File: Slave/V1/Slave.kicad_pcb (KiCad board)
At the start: 2 copper layers, 526 parts, among them J101 649002227222, J102 649002227222, J1301 649002227222, J1701 649002227222, J201 Header_Male_Pin_2.54mm_1X6_,_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, J202 Header_Male_Pin_2.54mm_1X3_,_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, J2101 649002227222, J2501 649002227222, J2901 649002227222, J300 Header_Male_Pin_2.54mm_1X2_,_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, J3301 649002227222, J401 649006227222, J402 649006227222, J501 649002227222, J901 649002227222, Q101 2N7002P,215, Q1201 CPH6347-TL-W, Q1202 BSS806NH6327XTSA1, Q1301 CPH6347-TL-W, Q1302 CPH6347-TL-W, Q1601 CPH6347-TL-W, Q1602 BSS806NH6327XTSA1, Q1701 CPH6347-TL-W, Q1702 CPH6347-TL-W, Q2001 CPH6347-TL-W, Q2002 BSS806NH6327XTSA1, Q2101 CPH6347-TL-W, Q2102 CPH6347-TL-W, Q2401 CPH6347-TL-W, Q2402 BSS806NH6327XTSA1, Q2501 CPH6347-TL-W, Q2502 CPH6347-TL-W, Q2801 CPH6347-TL-W, Q2802 BSS806NH6327XTSA1, Q2901 CPH6347-TL-W, Q2902 CPH6347-TL-W, Q3201 CPH6347-TL-W, Q3202 BSS806NH6327XTSA1, Q3301 CPH6347-TL-W, Q3302 CPH6347-TL-W, Q3601 CPH6347-TL-W, Q3602 BSS806NH6327XTSA1, Q501 CPH6347-TL-W, Q502 CPH6347-TL-W, Q801 CPH6347-TL-W, Q802 BSS806NH6327XTSA1, Q901 CPH6347-TL-W, Q902 CPH6347-TL-W, SW201 PTS645SM43SMTR92, SW202 PTS645SM43SMTR92, U1001 AP3015KTR-G1, U1002 AP2202K-ADJTRG1, U1101 ADC121S021CIMF/NOPB, U1201 ADCMP350YKSZ-REEL7, U1301 LTV-816S, U1302 SI8641AB-B-IS1, U1401 AP3015KTR-G1, U1402 AP2202K-ADJTRG1, U1501 ADC121S021CIMF/NOPB, U1601 ADCMP350YKSZ-REEL7, U1701 LTV-816S, U1702 SI8641AB-B-IS1, U1801 AP3015KTR-G1, U1802 AP2202K-ADJTRG1, U1901 ADC121S021CIMF/NOPB, U2001 ADCMP350YKSZ-REEL7, U201 STM32F446RE, U2101 LTV-816S, U2102 SI8641AB-B-IS1, U2201 AP3015KTR-G1, U2202 AP2202K-ADJTRG1, U2301 ADC121S021CIMF/NOPB, U2401 ADCMP350YKSZ-REEL7, U2501 LTV-816S, U2502 SI8641AB-B-IS1, U2601 AP3015KTR-G1, U2602 AP2202K-ADJTRG1, U2701 ADC121S021CIMF/NOPB, U2801 ADCMP350YKSZ-REEL7, U2901 LTV-816S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

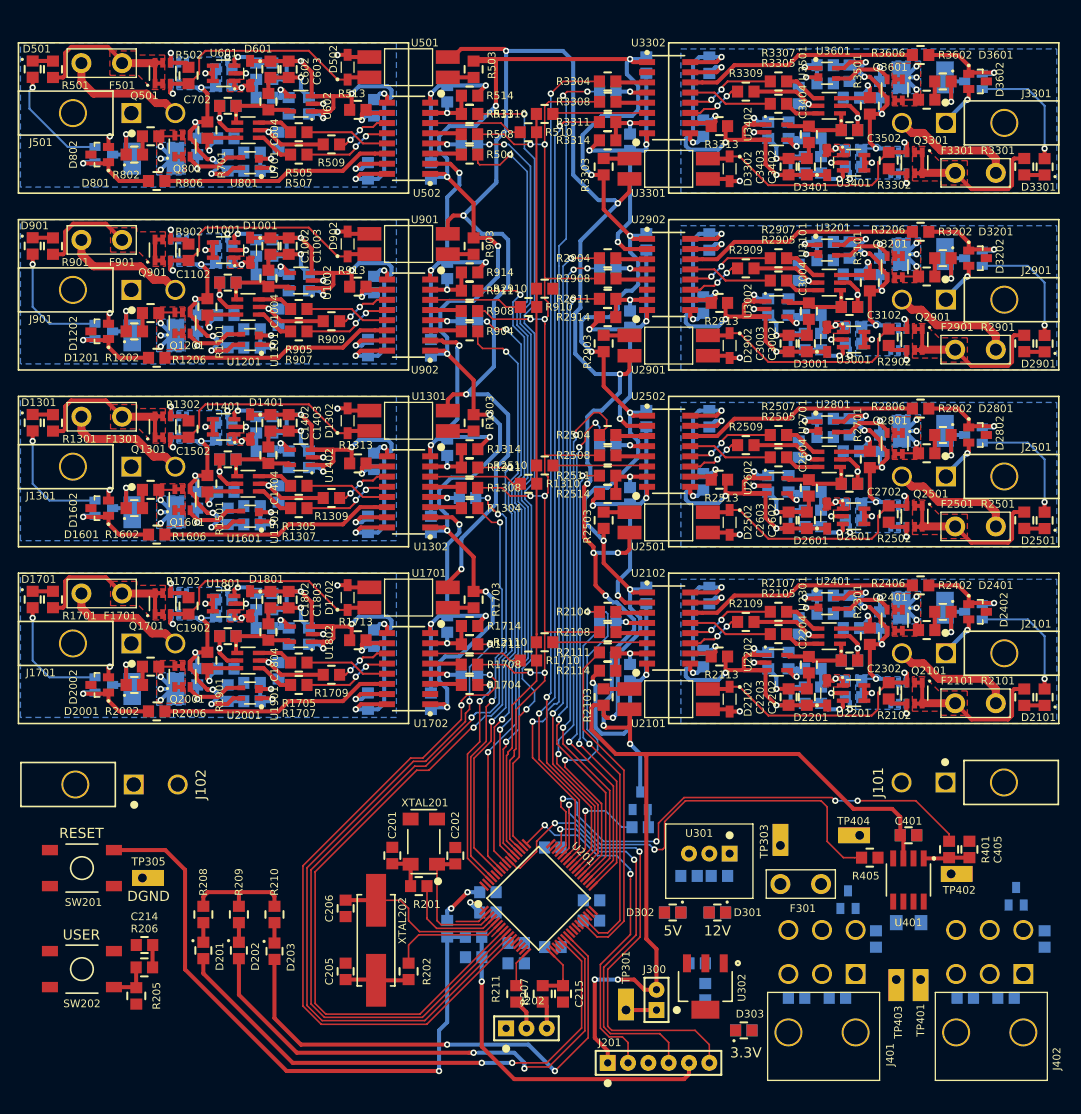
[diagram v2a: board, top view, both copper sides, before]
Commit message: Routing done, DRC almost clean
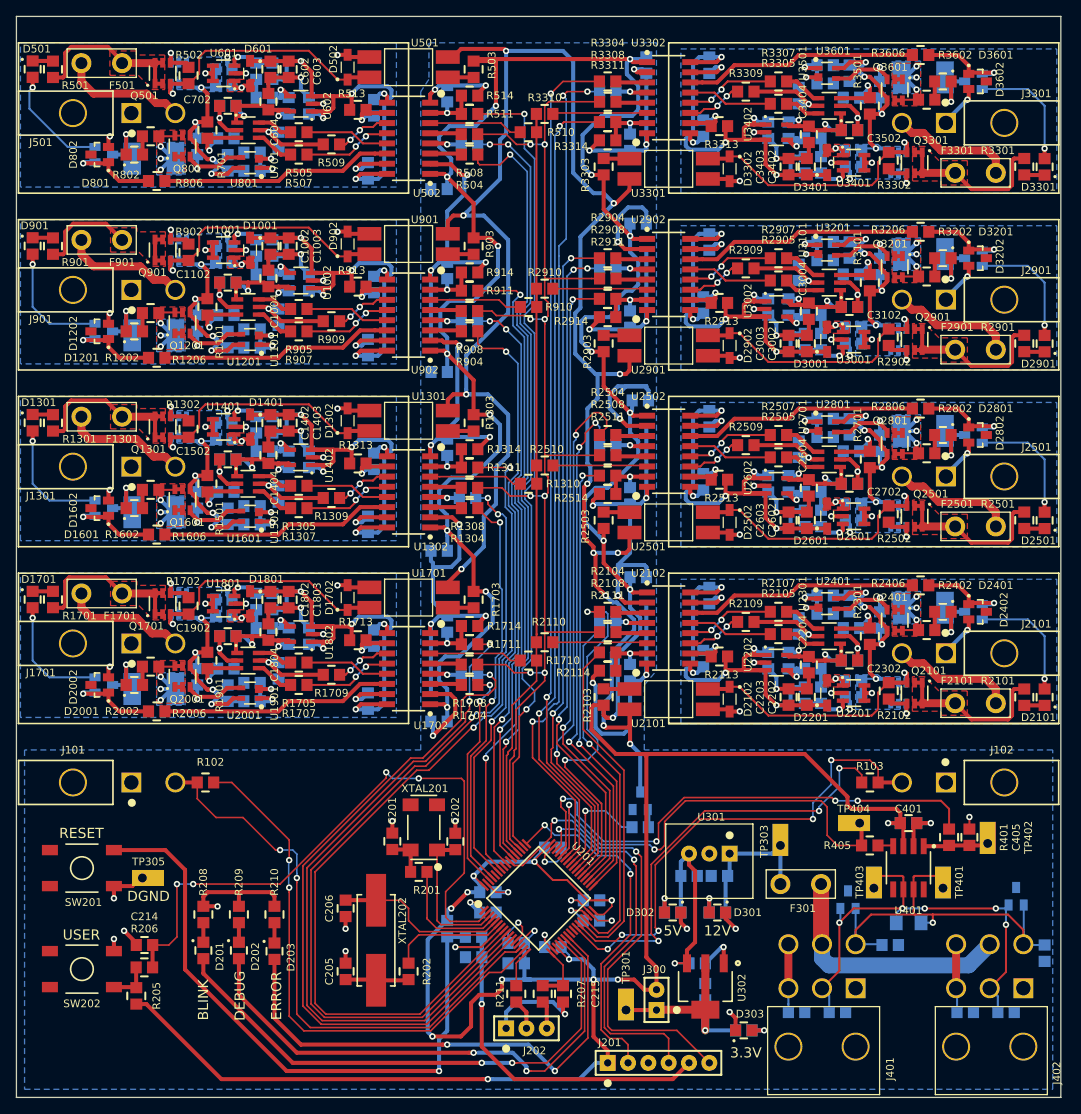
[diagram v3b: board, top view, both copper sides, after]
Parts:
- added R102: RC0805JR-0733KL, Resistors:R0805, F.Cu at (110.7, 138.7)
- added R103: RC0805JR-0733KL, Resistors:R0805, F.Cu at (195.9, 138.7)
- moved J101 116.4 mm to (95.2, 138.7), turned to 270 degrees
- moved J102 116.1 mm to (211.6, 138.7), turned to 90 degrees
- moved TP403 11.8 mm to (195.3, 151.9), turned to 90 degrees
- moved TP401 11.8 mm to (204.0, 151.9), turned to 90 degrees
- moved TP402 5.95 mm to (209.6, 146.3), turned to 90 degrees
- moved C1302 3.06 mm to (142.0, 109.7), turned to 180 degrees
- moved C902 2.87 mm to (142.0, 87.4), turned to 180 degrees
- moved C402 2.83 mm to (198.4, 159.0), turned to 180 degrees
- moved C1702 2.53 mm to (142.0, 131.1), turned to 180 degrees
- moved C2902 2.40 mm to (164.8, 68.8), turned to 0 degrees
- moved C502 2.39 mm to (142.0, 64.5), turned to 180 degrees
- moved C2102 2.39 mm to (164.8, 113.0), turned to 0 degrees
- moved C2502 2.17 mm to (165.1, 90.9), turned to 0 degrees
- moved C201 1.78 mm to (135.1, 145.0)
- moved J401 1.78 mm to (188.8, 171.7)
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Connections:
- J101 pad 1: Net-(J101-Pad1) -> DGND
- J101 pad 2: Net-(J101-Pad2) -> /NTC_1_ADC
- J102 pad 1: Net-(J102-Pad1) -> DGND
- J102 pad 2: Net-(J102-Pad2) -> /NTC_2_ADC
- U201 pad 14: /PA0 -> /NTC_1_ADC
- U201 pad 15: /PA1 -> /NTC_1_GPIO
- U201 pad 26: /PB0 -> /NTC_2_GPIO
- U201 pad 27: /PB1 -> /NTC_2_ADC
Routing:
- net VDD: track 390.9 -> 551.3 mm, vias 20 -> 29
- net DGND: track 276.3 -> 380.1 mm, vias 22 -> 45
- net /NTC_1_ADC: track 0.00 -> 72.9 mm, vias 0 -> 2
- net /STM32F446/USER_BTN: track 7.07 -> 79.2 mm, vias 0 -> 4
- net /NTC_1_GPIO: track 0.00 -> 68.8 mm, vias 0 -> 2
- net /CAN1/CAN_N: track 0.00 -> 62.8 mm, vias 0 -> 5
- net /NTC_2_ADC: track 0.00 -> 61.1 mm, vias 0 -> 4
- net /NTC_2_GPIO: track 0.00 -> 56.0 mm, vias 0 -> 4
- net /CAN1/CAN_P: track 0.00 -> 54.3 mm, vias 0 -> 1
- net CAN_PWR: track 0.00 -> 31.9 mm
- net 5V: track 0.00 -> 25.5 mm, vias 0 -> 1
- net 3.3V: track 3.81 -> 25.9 mm, vias 0 -> 1
- net 12V: track 0.00 -> 19.2 mm
- net Net-(R2910-Pad1): track 0.00 -> 11.8 mm
- net /CAN1/Shield2: track 0.00 -> 8.53 mm
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- added copper zone on B.Cu, net DGND
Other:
- board outline added: 130.6 x 135.1 mm
- board text added: "BLINK"
- board text added: "DEBUG"
- board text added: "ERROR"
- board text added: "ISOLATION"

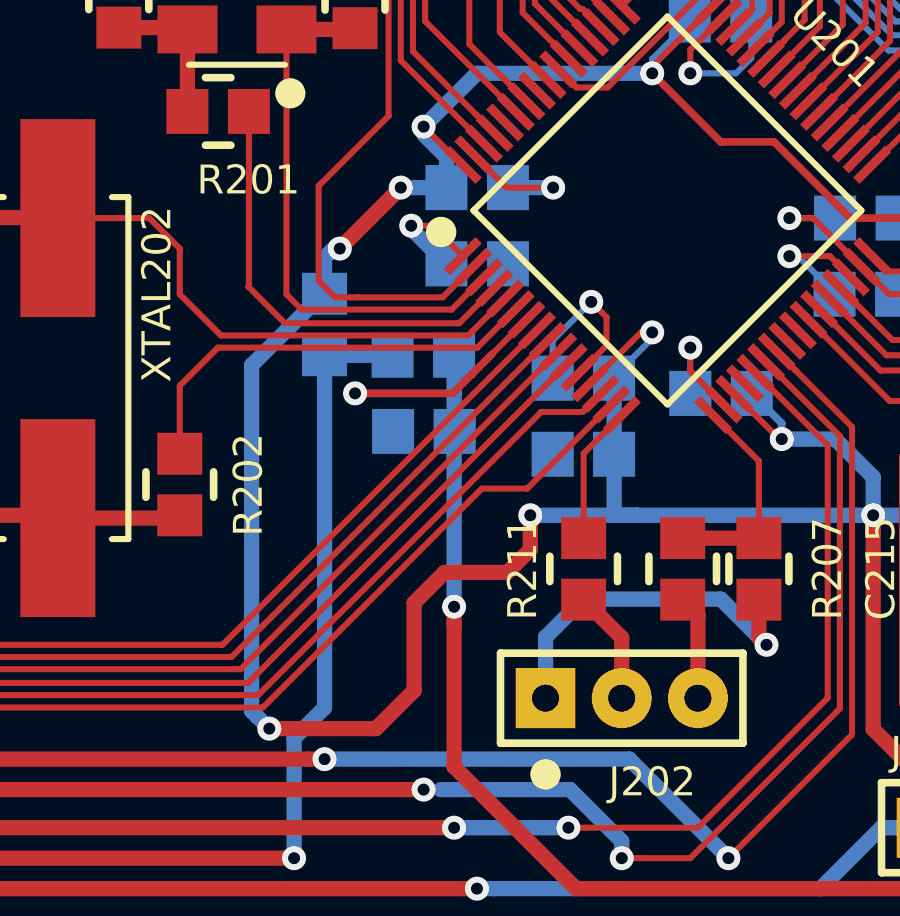
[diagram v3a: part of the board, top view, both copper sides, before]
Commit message: add cutout next to crystals, DRC clean
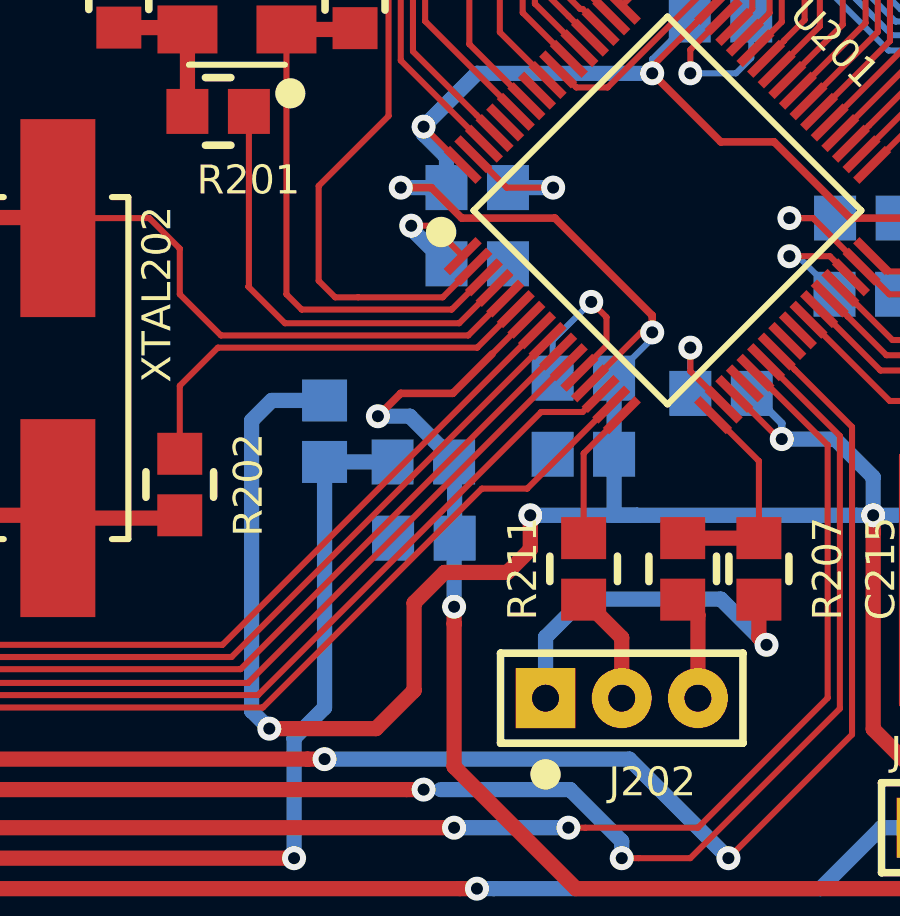
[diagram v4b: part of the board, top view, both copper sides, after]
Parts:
- moved C210 3.56 mm to (146.3, 164.1)
- moved R203 3.56 mm to (142.0, 161.5)
- moved R204 3.56 mm to (144.3, 161.5)
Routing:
- net /NRST: track 52.2 -> 48.1 mm
- net Net-(R203-Pad1): track 78.8 -> 75.3 mm
- net VDD: track 551.3 -> 554.8 mm, vias 29 -> 28
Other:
- net class Default: clearance 0.2032 -> 0.1524
- rule trace_clearance: 0.2032 -> 0.1524

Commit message: DRC Clean
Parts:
- added REF**: Pad TH 0.9mm, Connectors:PAD_TH_0.9mm, F.Cu at (211.8, 148.8)
- added REF**: Pad TH 0.9mm, Connectors:PAD_TH_0.9mm, F.Cu at (211.8, 43.1)
- added REF**: Pad TH 0.9mm, Connectors:PAD_TH_0.9mm, F.Cu at (92.4, 43.1)
- added REF**: Pad TH 0.9mm, Connectors:PAD_TH_0.9mm, F.Cu at (93.7, 172.7)
- moved TP402 3.53 mm to (207.8, 149.4), turned to 270 degrees
- moved D402 2.40 mm to (214.4, 154.9), turned to 90 degrees
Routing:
- net /CAN1/CAN_P: track 54.3 -> 52.9 mm
- net /CAN1/CAN_N: track 62.8 -> 63.9 mm
- net Net-(C405-Pad2): track 8.15 -> 8.76 mm
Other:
- board size 130.6 x 135.1 mm -> 130.6 x 138.2 mm

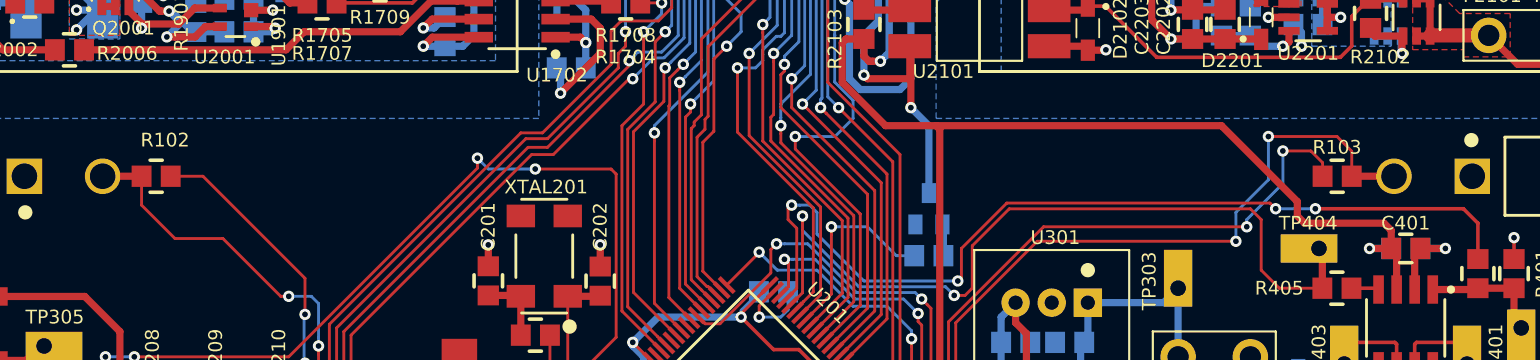
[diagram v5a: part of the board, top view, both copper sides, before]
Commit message: add capacitor to Temperature reading
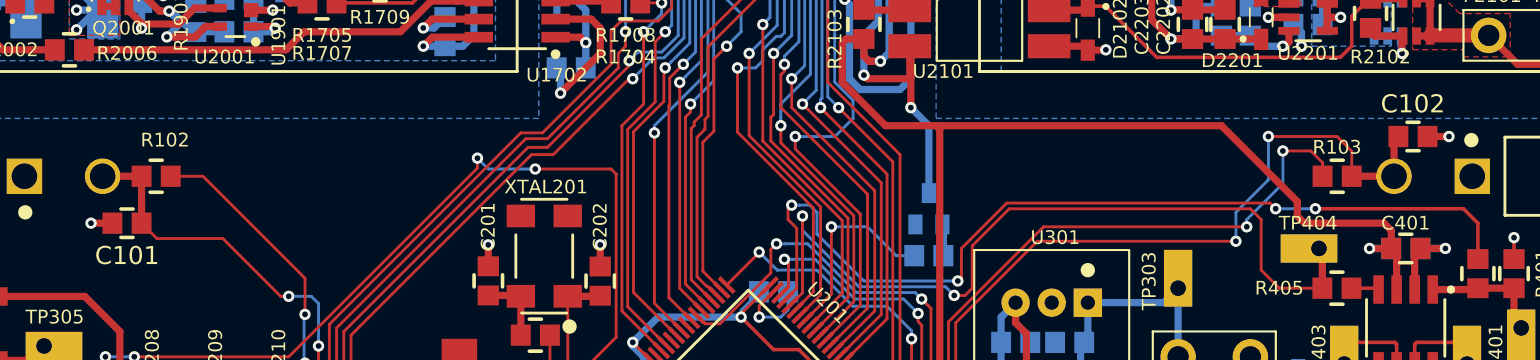
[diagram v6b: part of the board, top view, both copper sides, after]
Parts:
- added C101: 885012107015, Capacitors:C0805, F.Cu at (108.7, 142.0)
- added C102: 885012107015, Capacitors:C0805, F.Cu at (201.2, 135.9)
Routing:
- net DGND: track 380.1 -> 383.1 mm, vias 45 -> 47
- net /NTC_2_ADC: track 61.1 -> 64.0 mm
- net /NTC_1_ADC: track 72.9 -> 73.6 mm
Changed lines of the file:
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@@
 (kicad_pcb (version 4) (host pcbnew 4.0.5+dfsg1-4)
   (general
-    (links 1118)
-    (no_connects 0)
+    (links 1122)
+    (no_connects 3)
     (area 88.087999 39.827999 218.744001 178.104001)
     (thickness 1.6)
     (drawings 108)
-    (tracks 4357)
+    (tracks 4363)
     (zones 0)
-    (modules 532)
+    (modules 534)
     (nets 361)
   )
@@
     (pad 1 thru_hole circle (at 0.29 0.01) (size 4 4) (drill 3.5) (layers *.Cu *.Mask))
   )
+  (module Capacitors:C0805 (layer F.Cu)
+    (at 108.694 141.986)
+    (fp_text reference C101 (at 1.034 2.286) (layer F.SilkS)
+      (effects (font (size 1.27 1.27) (thickness 0.2032)))
+    )
+    (fp_text value 885012107015 (at 1.73 2.33) (layer F.Fab) hide
+      (effects (font (size 1.27 1.27) (thickness 0.254)))
+    )
+    (fp_line (start 0.6 -1) (end 1.45 -1) (layer F.SilkS) (width 0.254))
+    (fp_line (start 0.6 1) (end 1.45 1) (layer F.SilkS) (width 0.254))
+    (pad 1 smd rect (at 0 0) (size 1.4 1.5) (layers F.Cu F.Paste F.Mask)
+      (net 1 DGND))
+    (pad 2 smd rect (at 2.05 0) (size 1.4 1.5) (layers F.Cu F.Paste F.Mask)
+      (net 357 /NTC_1_ADC))
+    (model Capacitors/C0805.wrl
+      (at (xyz 0.04 0.0005 0))
+      (scale (xyz 0.3937 0.3937 0.3937))
+      (rotate (xyz 0 0 0))
+    )
+  )
+  (module Capacitors:C0805 (layer F.Cu)
+    (at 201.186 135.89 180)
+    (fp_text reference C102 (at 1.034 2.286 180) (layer F.SilkS)
+      (effects (font (size 1.27 1.27) (thickness 0.2032)))
+    )
+    (fp_text value 885012107015 (at 1.73 2.33 180) (layer F.Fab) hide
+      (effects (font (size 1.27 1.27) (thickness 0.254)))
+    )
+    (fp_line (start 0.6 -1) (end 1.45 -1) (layer F.SilkS) (width 0.254))
+    (fp_line (start 0.6 1) (end 1.45 1) (layer F.SilkS) (width 0.254))
+    (pad 1 smd rect (at 0 0 180) (size 1.4 1.5) (layers F.Cu F.Paste F.Mask)
+      (net 1 DGND))
+    (pad 2 smd rect (at 2.05 0 180) (size 1.4 1.5) (layers F.Cu F.Paste F.Mask)
+      (net 358 /NTC_2_ADC))
+    (model Capacitors/C0805.wrl
+      (at (xyz 0.04 0.0005 0))
+      (scale (xyz 0.3937 0.3937 0.3937))
+      (rotate (xyz 0 0 0))
+    )
+  )
   (dimension 130.556 (width 0.2032) (layer Eco1.User)
     (gr_text "130.556 mm" (at 153.416 34.2646) (layer Eco1.User)
@@
   (gr_line (start 137.16 65.024) (end 88.392 65.024) (layer F.SilkS) (width 0.2))
   (gr_line (start 137.16 46.228) (end 137.16 65.024) (layer F.SilkS) (width 0.2))
+  (segment (start 108.694 141.986) (end 107.188 141.986) (width 0.508) (layer F.Cu) (net 1))
+  (segment (start 201.186 135.89) (end 202.692 135.89) (width 0.508) (layer F.Cu) (net 1))
+  (via (at 202.692 135.89) (size 0.8) (drill 0.4) (layers F.Cu B.Cu) (net 1))
+  (via (at 107.188 141.986) (size 0.8) (drill 0.4) (layers F.Cu B.Cu) (net 1))
   (segment (start 163.322 115.316) (end 163.322 111.506) (width 0.508) (layer B.Cu) (net 1))
   (segment (start 163.322 111.506) (end 164.846 109.982) (width 0.508) (layer B.Cu) (net 1))
@@
   (segment (start 195.834 146.558) (end 197.645 146.558) (width 0.254) (layer F.Cu) (net 355))
   (segment (start 197.645 146.558) (end 197.739 146.652) (width 0.254) (layer F.Cu) (net 355))
+  (segment (start 110.744 141.986) (end 110.744 138.684) (width 0.508) (layer F.Cu) (net 357))
+  (segment (start 121.0945 147.1295) (end 120.528815 147.1295) (width 0.2032) (layer F.Cu) (net 357))
+  (segment (start 120.528815 147.1295) (end 116.464815 143.0655) (width 0.2032) (layer F.Cu) (net 357))
+  (segment (start 116.464815 143.0655) (end 111.8235 143.0655) (width 0.2032) (layer F.Cu) (net 357))
+  (segment (start 111.8235 143.0655) (end 110.744 141.986) (width 0.2032) (layer F.Cu) (net 357))
   (segment (start 121.0945 147.1295) (end 122.682 147.1295) (width 0.2032) (layer B.Cu) (net 357))
   (segment (start 122.682 147.1295) (end 123.190026 147.637526) (width 0.2032) (layer B.Cu) (net 357))
@@
   (segment (start 151.188614 159.278474) (end 150.587574 159.879514) (width 0.2032) (layer F.Cu) (net 357))
   (segment (start 150.587574 159.879514) (end 149.20696 159.879514) (width 0.2032) (layer F.Cu) (net 357))
-  (segment (start 113.0935 143.0655) (end 110.744 140.716) (width 0.2032) (layer F.Cu) (net 357))
-  (segment (start 110.744 140.716) (end 110.744 138.684) (width 0.2032) (layer F.Cu) (net 357))
-  (segment (start 116.464815 143.0655) (end 113.0935 143.0655) (width 0.2032) (layer F.Cu) (net 357))
-  (segment (start 121.0945 147.1295) (end 120.528815 147.1295) (width 0.2032) (layer F.Cu) (net 357))
-  (segment (start 120.528815 147.1295) (end 116.464815 143.0655) (width 0.2032) (layer F.Cu) (net 357))
   (via (at 121.0945 147.1295) (size 0.8) (drill 0.4) (layers F.Cu B.Cu) (net 357))
   (segment (start 110.744 138.684) (end 108.05 138.684) (width 0.508) (layer F.Cu) (net 357))
+  (segment (start 198.826 138.684) (end 198.826 136.2) (width 0.508) (layer F.Cu) (net 358))
+  (segment (start 198.826 136.2) (end 199.136 135.89) (width 0.508) (layer F.Cu) (net 358))
   (segment (start 187.706 143.256) (end 173.736 143.256) (width 0.2032) (layer F.Cu) (net 358))
   (segment (start 173.736 143.256) (end 168.002001 148.989999) (width 0.2032) (layer F.Cu) (net 358))

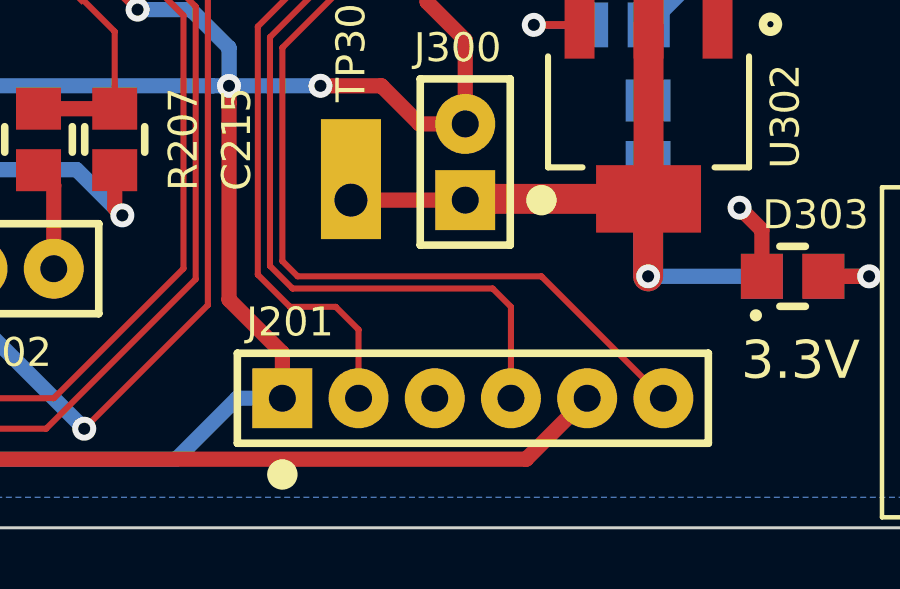
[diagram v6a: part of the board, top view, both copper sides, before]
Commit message: add SWD silkscreen
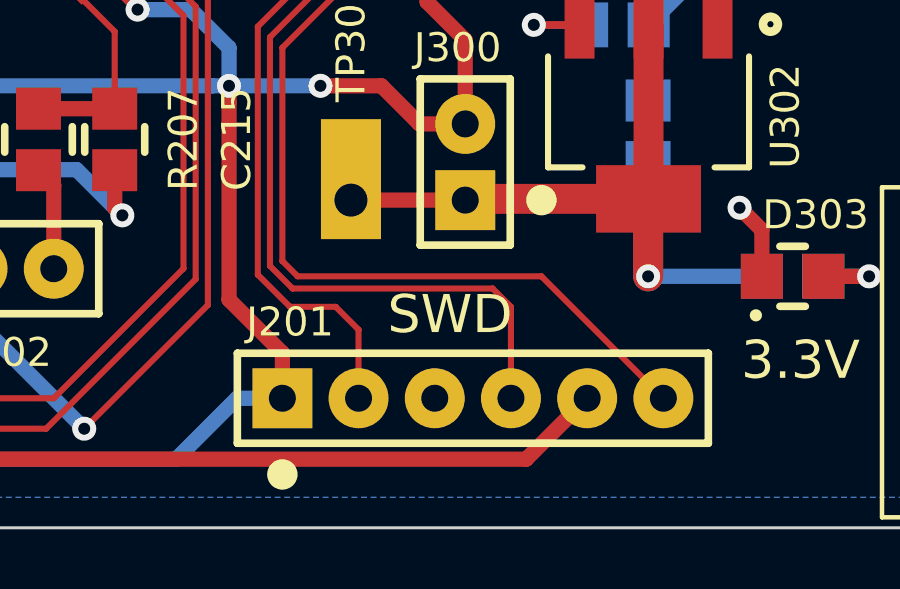
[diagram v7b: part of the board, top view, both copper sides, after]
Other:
- board text added: "SWD"
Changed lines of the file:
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@@
   (general
     (links 1122)
-    (no_connects 3)
+    (no_connects 0)
     (area 88.087999 39.827999 218.744001 178.104001)
     (thickness 1.6)
-    (drawings 108)
+    (drawings 109)
     (tracks 4363)
     (zones 0)
@@
   )
   (setup
-    (last_trace_width 0.508)
+    (last_trace_width 0.2032)
     (user_trace_width 0.127)
     (user_trace_width 0.18)
@@
     )
   )
+  (gr_text SWD (at 167.64 170.942) (layer F.SilkS)
+    (effects (font (size 1.27 1.27) (thickness 0.2032)))
+  )
   (dimension 130.556 (width 0.2032) (layer Eco1.User)
